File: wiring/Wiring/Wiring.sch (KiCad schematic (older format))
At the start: 6 parts, among them U1 MAIN, U2 E, U3 F, U4 G

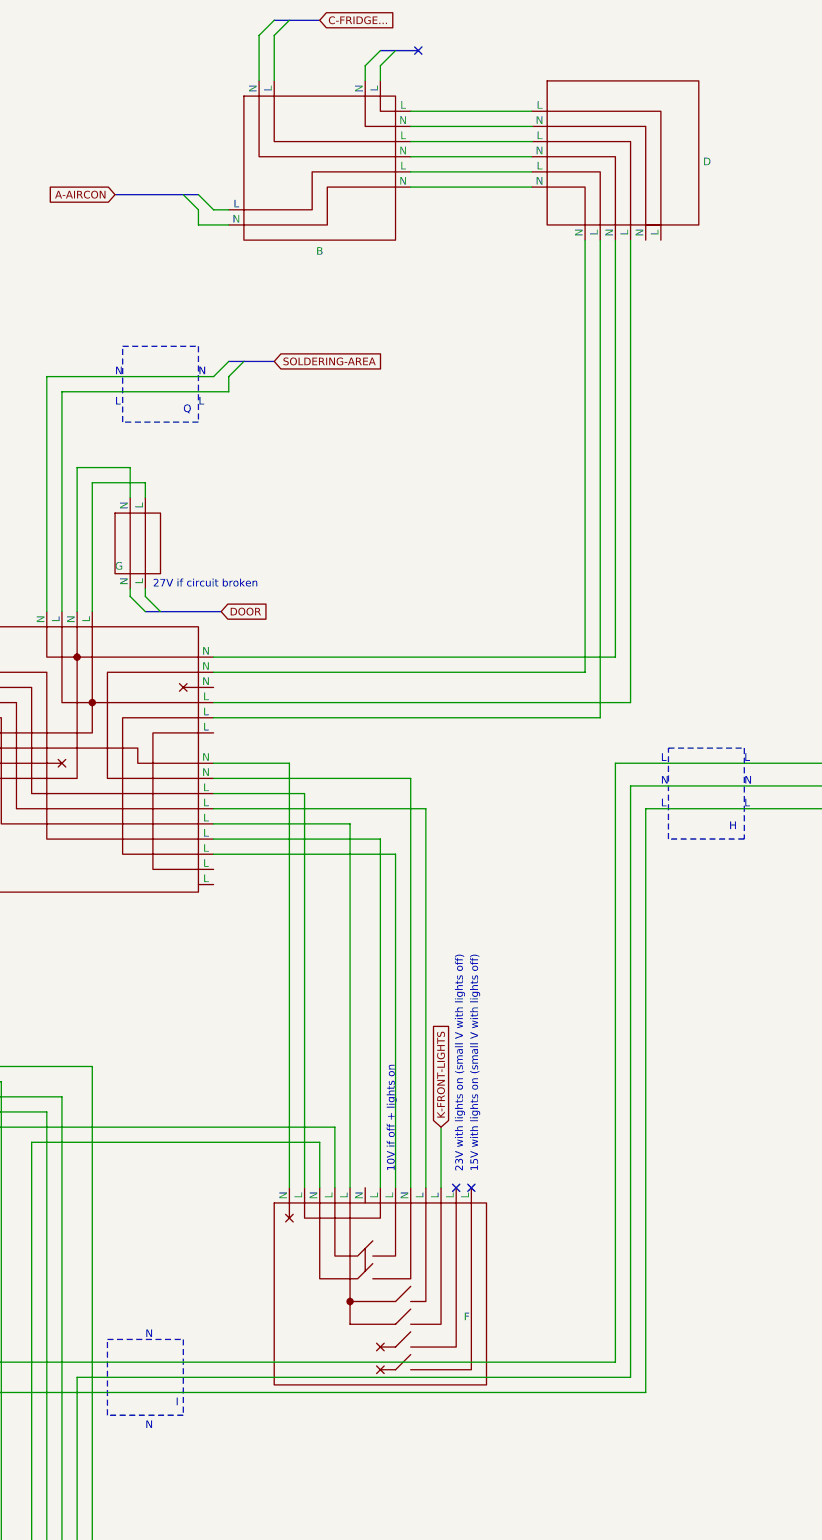
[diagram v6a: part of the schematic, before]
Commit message: Add U, plus wiring
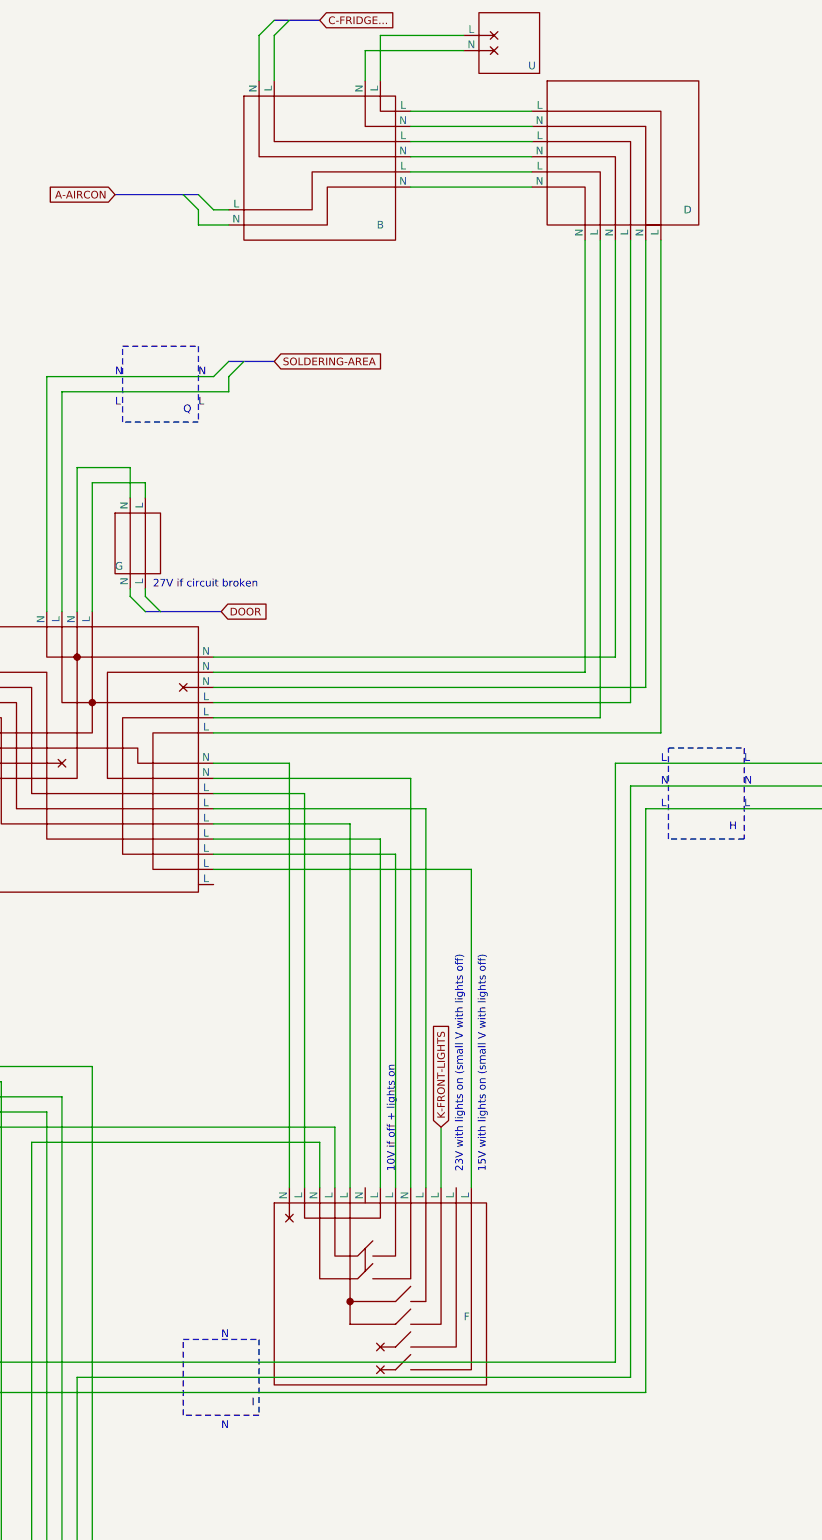
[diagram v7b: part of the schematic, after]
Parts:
- added U?: U, symbol Wiring:U
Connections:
- net at U3.~ (L): now also U2.24 (L)
- net at U2.12 (N): now also U?.10 (N)
- net at U2.14 (L): now also U?.12 (L)
- net at U?.~ (N): now also U?.12 (L)
- new net: U2.14 (L), U?.12 (L)
- new net: U?.10 (N), U?.8 (N) (x2)
- new net: U?.12 (L), U?.9 (L) (x2)
- new net: U?.10 (N), U?.~ (N)
- no-connect marks 3 -> 0
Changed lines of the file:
@@
 Text GLabel 13000 8000 1    50   Input ~ 0
 K-FRONT-LIGHTS
-NoConn ~ 13200 8400
 Text Notes 12700 8300 1    50   ~ 0
 10V if off + lights on
-NoConn ~ 13100 8400
 Text Notes 13150 8300 1    50   ~ 0
 23V with lights on (small V with lights off)
-Text Notes 13250 8300 1    50   ~ 0
-15V with lights on (small V with lights off)
 Wire Wire Line
 	10300 8100 12200 8100
@@
 	16950 5700 16950 5600
 Wire Notes Line
-	10800 9400 11300 9400
-Wire Notes Line
-	11300 9900 10800 9900
-Wire Notes Line
-	10800 9900 10800 9400
-Text Notes 11250 9850 0    50   ~ 0
+	11300 9400 11800 9400
+Wire Notes Line
+	11800 9900 11300 9900
+Wire Notes Line
+	11300 9900 11300 9400
+Text Notes 11750 9850 0    50   ~ 0
 I
 Wire Wire Line
@@
 Text Notes 14450 5900 0    50   ~ 0
 L
-Text Notes 11050 9400 0    50   ~ 0
-N
-Text Notes 11050 10000 0    50   ~ 0
+Text Notes 11550 9400 0    50   ~ 0
+N
+Text Notes 11550 10000 0    50   ~ 0
 N
 Text GLabel 17250 6000 2    50   Input ~ 0
@@
 	8900 5000 8900 9550
 Wire Notes Line
-	11300 9400 11300 9900
+	11800 9400 11800 9900
 Wire Wire Line
 	8900 9550 14150 9550
@@
 P 12200 1650
 F 0 "U?" H 11650 2150 50  0001 C CNN
-F 1 "B" H 12200 1077 50  0000 C CNN
+F 1 "B" H 12600 1250 50  0000 C CNN
 F 2 "" H 11500 1500 50  0001 C CNN
 F 3 "" H 11500 1500 50  0001 C CNN
@@
 	1    0    0    -1
 $EndComp
-Wire Wire Line
-	12500 1100 12500 1000
-Wire Wire Line
-	12600 1100 12600 1000
-Entry Wire Line
-	12500 1000 12600 900
-Entry Wire Line
-	12600 1000 12700 900
-NoConn ~ 12850 900
 Wire Wire Line
 	10950 3650 10600 3650
@@
 P 14200 1550
 F 0 "U?" H 13650 2050 50  0001 C CNN
-F 1 "D" H 14728 1467 50  0000 L CNN
+F 1 "D" H 14600 1150 50  0000 L CNN
 F 2 "" H 13500 2050 50  0001 C CNN
 F 3 "" H 13500 2050 50  0001 C CNN
@@
 Wire Wire Line
 	12800 1400 13600 1400
-Wire Bus Line
-	10850 1850 11400 1850
-Wire Bus Line
-	12600 900  12850 900
-Wire Bus Line
-	11600 2950 11900 2950
-Wire Bus Line
-	16900 6000 17250 6000
-Wire Bus Line
-	16900 5500 17250 5500
-Wire Bus Line
-	11900 700  12200 700
-Wire Bus Line
-	11050 4600 11550 4600
 $Comp
 L Wiring:E U2
@@
 	1    0    0    -1
 $EndComp
+$Comp
+L Wiring:U U?
+U 1 1 5EE3602B
+P 13450 850
+F 0 "U?" H 13300 1000 50  0001 C CNN
+F 1 "U" H 13300 1000 50  0000 C CNN
+F 2 "" H 12750 700 50  0001 C CNN
+F 3 "" H 12750 700 50  0001 C CNN
+	1    13450 850
+	-1   0    0    1
+$EndComp
+Text Notes 13300 8300 1    50   ~ 0
+15V with lights on (small V with lights off)
+Wire Wire Line
+	14450 5400 14450 2150
+Wire Wire Line
+	13150 900  12500 900
+Wire Wire Line
+	12500 900  12500 1100
+Wire Wire Line
+	12600 1100 12600 800
+Wire Wire Line
+	12600 800  13150 800
+Wire Wire Line
+	14350 2150 14350 5100
+Wire Wire Line
+	11500 5100 14350 5100
+Wire Wire Line
+	13200 8400 13200 6300
+Wire Wire Line
+	13200 6300 11500 6300
+Wire Wire Line
+	11500 5400 14450 5400
+Wire Bus Line
+	10850 1850 11400 1850
+Wire Bus Line
+	11600 2950 11900 2950
+Wire Bus Line
+	16900 6000 17250 6000
+Wire Bus Line
+	16900 5500 17250 5500
+Wire Bus Line
+	11900 700  12200 700
+Wire Bus Line
+	11050 4600 11550 4600
 $EndSCHEMATC

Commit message: Add V
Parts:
- added U?: I, symbol Wiring:I
- added U?: V, symbol Wiring:V
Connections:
- net at U3.12 (L): now also U?.~ (N)
- net at U1.~ (N): now also U?.16 (N)
- net at U?.~ (N): now also U?.12 (L)
- new net: U2.14 (L), U?.12 (L)
- new net: U?.10 (N), U?.8 (N) (x2)
- new net: U?.12 (L), U?.9 (L) (x2)
- new net: U?.10 (N), U?.~ (N)
- new net: U?.12 (L), U?.~ (N)
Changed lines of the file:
@@
 P 12550 8850
 F 0 "U3" H 13178 8929 50  0001 L CNN
-F 1 "F" H 13150 8450 50  0000 L CNN
+F 1 "F" H 13250 8050 50  0000 L CNN
 F 2 "Package_DFN_QFN:DFN-8-1EP_4x4mm_P0.8mm_EP2.5x3.6mm" H 12500 9000 50  0001 C CNN
 F 3 "" H 12500 9000 50  0001 C CNN
@@
 27V if circuit broken
 Wire Notes Line
-	14500 5500 15000 5500
-Wire Notes Line
-	15000 5500 15000 6100
-Wire Notes Line
-	14500 6100 14500 5500
-Text Notes 14900 6050 0    50   ~ 0
+	15600 6750 16100 6750
+Wire Notes Line
+	16100 6750 16100 7350
+Wire Notes Line
+	15600 7350 15600 6750
+Text Notes 16000 7300 0    50   ~ 0
 H
 Wire Notes Line
-	16000 5500 16500 5500
-Wire Notes Line
-	16500 5500 16500 6100
-Wire Notes Line
-	16500 6100 16000 6100
-Wire Notes Line
-	16000 6100 16000 5500
-Text Notes 16450 6050 0    50   ~ 0
+	17100 6750 17600 6750
+Wire Notes Line
+	17600 6750 17600 7350
+Wire Notes Line
+	17600 7350 17100 7350
+Wire Notes Line
+	17100 7350 17100 6750
+Text Notes 17550 7300 0    50   ~ 0
 J
-Text GLabel 17250 5500 2    50   Input ~ 0
+Text GLabel 18350 6750 2    50   Input ~ 0
 ROUTER
 Entry Wire Line
-	16800 5600 16900 5500
-Wire Wire Line
-	16800 5600 14150 5600
-Wire Wire Line
-	14250 9650 14250 5750
-Entry Wire Line
-	17050 5500 16950 5600
-Wire Wire Line
-	16950 5700 16950 5600
-Wire Notes Line
-	11300 9400 11800 9400
-Wire Notes Line
-	11800 9900 11300 9900
-Wire Notes Line
-	11300 9900 11300 9400
-Text Notes 11750 9850 0    50   ~ 0
+	17900 6850 18000 6750
+Entry Wire Line
+	18150 6750 18050 6850
+Wire Wire Line
+	18050 6950 18050 6850
+Wire Notes Line
+	11250 9750 11750 9750
+Wire Notes Line
+	11750 10250 11250 10250
+Wire Notes Line
+	11250 10250 11250 9750
+Text Notes 11700 10200 0    50   ~ 0
 I
 Wire Wire Line
 	12900 5900 12900 8400
 Wire Notes Line
-	15000 6100 14500 6100
-Wire Wire Line
-	16250 5700 16950 5700
-Wire Wire Line
-	16250 5750 16250 5700
-Wire Wire Line
-	14250 5750 16250 5750
-Wire Wire Line
-	16250 5750 16250 5800
-Wire Wire Line
-	16250 5800 16950 5800
-Connection ~ 16250 5750
-Text Notes 16500 5600 0    50   ~ 0
-L
-Text Notes 16500 5700 0    50   ~ 0
-N
-Text Notes 16500 5800 0    50   ~ 0
-N
-Text Notes 16500 5900 0    50   ~ 0
-L
-Text Notes 15950 5600 0    50   ~ 0
-L
-Text Notes 15950 5750 0    50   ~ 0
-N
-Text Notes 15950 5900 0    50   ~ 0
-L
-Text Notes 15000 5600 0    50   ~ 0
-L
-Text Notes 15000 5900 0    50   ~ 0
-L
-Text Notes 15000 5750 0    50   ~ 0
-N
-Text Notes 14450 5750 0    50   ~ 0
-N
-Text Notes 14450 5600 0    50   ~ 0
-L
-Text Notes 14450 5900 0    50   ~ 0
-L
-Text Notes 11550 9400 0    50   ~ 0
-N
-Text Notes 11550 10000 0    50   ~ 0
-N
-Text GLabel 17250 6000 2    50   Input ~ 0
+	16100 7350 15600 7350
+Wire Wire Line
+	17350 6950 18050 6950
+Wire Wire Line
+	17350 7000 17350 6950
+Wire Wire Line
+	17350 7000 17350 7050
+Wire Wire Line
+	17350 7050 18050 7050
+Connection ~ 17350 7000
+Text Notes 17600 6850 0    50   ~ 0
+L
+Text Notes 17600 6950 0    50   ~ 0
+N
+Text Notes 17600 7050 0    50   ~ 0
+N
+Text Notes 17600 7150 0    50   ~ 0
+L
+Text Notes 17050 6850 0    50   ~ 0
+L
+Text Notes 17050 7000 0    50   ~ 0
+N
+Text Notes 17050 7150 0    50   ~ 0
+L
+Text Notes 16100 6850 0    50   ~ 0
+L
+Text Notes 16100 7150 0    50   ~ 0
+L
+Text Notes 16100 7000 0    50   ~ 0
+N
+Text Notes 15550 7000 0    50   ~ 0
+N
+Text Notes 15550 6850 0    50   ~ 0
+L
+Text Notes 15550 7150 0    50   ~ 0
+L
+Text GLabel 18350 7250 2    50   Input ~ 0
 BACK-LIGHTS
 Entry Wire Line
-	16800 5900 16900 6000
-Entry Wire Line
-	16950 5900 17050 6000
-Wire Wire Line
-	16950 5800 16950 5900
+	17900 7150 18000 7250
+Entry Wire Line
+	18050 7150 18150 7250
+Wire Wire Line
+	18050 7050 18050 7150
 Wire Wire Line
 	12300 8400 12300 8000
@@
 	10500 11450 10500 7800
 Wire Wire Line
-	10600 9650 10600 11450
+	10600 9900 10600 11450
 Wire Wire Line
 	9900 5600 9850 5600
@@
 	12900 5900 11500 5900
 Wire Wire Line
-	10600 9650 14250 9650
-Wire Wire Line
-	14350 5900 14350 9750
-Wire Wire Line
-	14350 5900 16800 5900
-Wire Wire Line
-	14150 5600 14150 9550
+	10600 9900 14250 9900
+Wire Wire Line
+	14350 7150 14350 10000
+Wire Wire Line
+	14150 6850 14150 9800
 Wire Wire Line
 	9900 5200 9000 5200
 Wire Wire Line
-	9000 5200 9000 9750
+	9000 5200 9000 10000
 Wire Wire Line
 	9900 5000 8900 5000
 Wire Wire Line
-	8900 5000 8900 9550
-Wire Notes Line
-	11800 9400 11800 9900
-Wire Wire Line
-	8900 9550 14150 9550
-Wire Wire Line
-	9000 9750 14350 9750
+	8900 5000 8900 9800
+Wire Notes Line
+	11750 9750 11750 10250
+Wire Wire Line
+	8900 9800 14150 9800
+Wire Wire Line
+	9000 10000 14350 10000
 Text Notes 9550 9400 0    50   ~ 0
 Route more\nwires through\nI! (WIP comp.)
@@
 Wire Wire Line
 	11500 5400 14450 5400
+$Comp
+L Wiring:I U?
+U 1 1 5EE80A79
+P 16600 3650
+F 0 "U?" H 17350 2700 50  0001 C CNN
+F 1 "I" H 17250 2800 50  0000 C CNN
+F 2 "" H 15900 3500 50  0001 C CNN
+F 3 "" H 15900 3500 50  0001 C CNN
+	1    16600 3650
+	1    0    0    -1
+$EndComp
+Wire Wire Line
+	14250 9900 14250 7000
+Wire Wire Line
+	13100 5500 17100 5500
+Wire Wire Line
+	17100 5500 17100 4650
+Wire Wire Line
+	13100 5500 13100 8400
+$Comp
+L Wiring:V U?
+U 1 1 5EE9031E
+P 16500 2300
+F 0 "U?" H 16350 2450 50  0001 C CNN
+F 1 "V" H 16558 2573 50  0000 C CNN
+F 2 "" H 15800 2150 50  0001 C CNN
+F 3 "" H 15800 2150 50  0001 C CNN
+	1    16500 2300
+	1    0    0    -1
+$EndComp
+Wire Wire Line
+	16800 2350 17100 2350
+Wire Wire Line
+	17100 2350 17100 2700
+Wire Wire Line
+	17000 2700 17000 2250
+Wire Wire Line
+	17000 2250 16800 2250
+Wire Wire Line
+	14550 2950 14550 10300
+Wire Wire Line
+	14550 10300 10800 10300
+Wire Wire Line
+	10800 10300 10800 11450
+Wire Wire Line
+	14150 6850 17900 6850
+Wire Wire Line
+	14250 7000 17350 7000
+Wire Wire Line
+	14350 7150 17900 7150
+Wire Wire Line
+	14550 2950 15800 2950
 Wire Bus Line
 	10850 1850 11400 1850
@@
 	11600 2950 11900 2950
 Wire Bus Line
-	16900 6000 17250 6000
+	18000 7250 18350 7250
 Wire Bus Line
-	16900 5500 17250 5500
+	18000 6750 18350 6750
 Wire Bus Line
 	11900 700  12200 700
